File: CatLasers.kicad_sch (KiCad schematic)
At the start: 3 parts, among them J2 Conn_01x04, J3 Conn_01x04, U2 ATTINY402-SSN

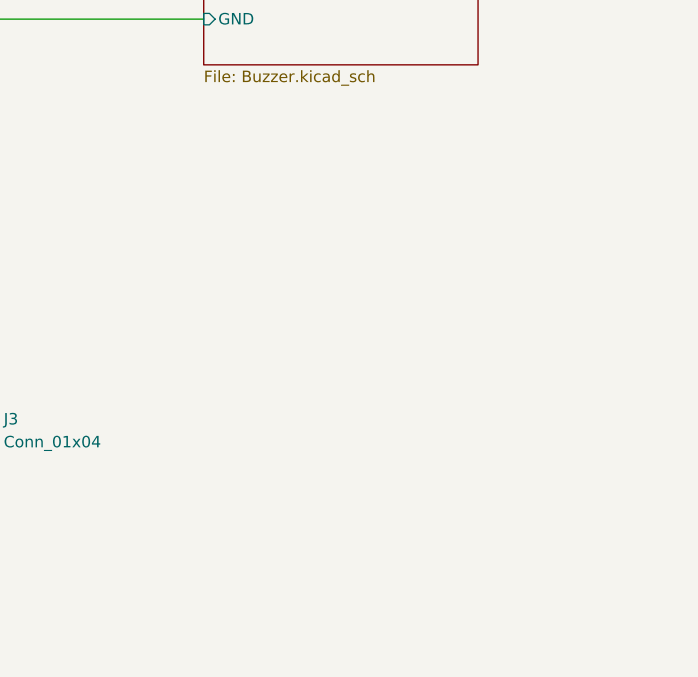
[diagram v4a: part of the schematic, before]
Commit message: IR Emitter circuit
Circuit added and all footprints assigned
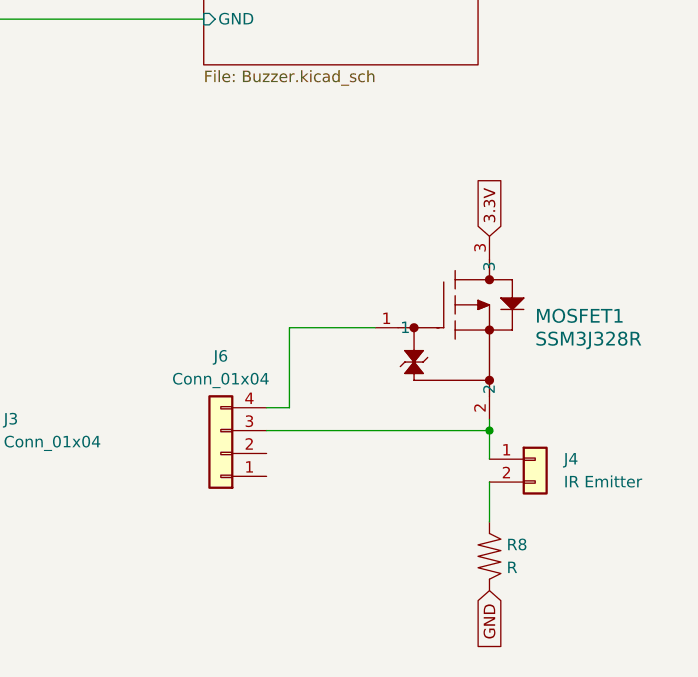
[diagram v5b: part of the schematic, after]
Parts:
- added J4: IR Emitter, Connector_PinHeader_2.54mm:PinHeader_1x02_P2.54mm_Vertical, symbol Connector_Generic:Conn_01x02
- added J6: Conn_01x04, Connector_PinHeader_2.54mm:PinHeader_1x04_P2.54mm_Vertical, symbol Connector_Generic:Conn_01x04
- added MOSFET1: SSM3J328R, SOT-23F_TOS, symbol ProjPMOS_LV:SSM3J328R
- added R8: R, Resistor_SMD:R_0805_2012Metric, symbol Hestres_Standard_Lib:R
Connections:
- net 3.3V: now also MOSFET1.3
- net GND: now also R8.2
- new net: J4.2 (Pin_2), R8.1
- new net: J6.4 (Pin_4), MOSFET1.1
- new net: J4.1 (Pin_1), J6.3 (Pin_3), MOSFET1.2
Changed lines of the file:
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@@
   (junction (at 80.645 42.545) (diameter 0) (color 0 0 0 0)
   )
+  (junction (at 179.705 101.6) (diameter 0) (color 0 0 0 0)
+  )
   (junction (at 114.935 55.88) (diameter 0) (color 0 0 0 0)
   )
@@
     (stroke (width 0) (type default))
   )
+  (wire (pts (xy 179.705 100.33) (xy 179.705 101.6))
+    (stroke (width 0) (type default))
+  )
+  (wire (pts (xy 154.94 99.06) (xy 157.48 99.06))
+    (stroke (width 0) (type default))
+  )
+  (wire (pts (xy 179.705 101.6) (xy 179.705 104.775))
+    (stroke (width 0) (type default))
+  )
+  (wire (pts (xy 154.94 101.6) (xy 179.705 101.6))
+    (stroke (width 0) (type default))
+  )
   (wire (pts (xy 72.39 49.53) (xy 76.835 49.53))
     (stroke (width 0) (type default))
@@
   )
   (wire (pts (xy 72.39 55.88) (xy 114.935 55.88))
+    (stroke (width 0) (type default))
+  )
+  (wire (pts (xy 157.48 99.06) (xy 157.48 90.17))
+    (stroke (width 0) (type default))
+  )
+  (wire (pts (xy 157.48 90.17) (xy 167.005 90.17))
+    (stroke (width 0) (type default))
+  )
+  (wire (pts (xy 179.705 107.315) (xy 179.705 111.76))
     (stroke (width 0) (type default))
   )
@@
     )
   )
+  (global_label "3.3V" (shape input) (at 179.705 80.01 90) (fields_autoplaced)
+    (effects (font (size 1.27 1.27)) (justify left))
+    (property "Intersheetrefs" "${INTERSHEET_REFS}" (at 179.705 72.9124 90)
+      (effects (font (size 1.27 1.27)) (justify left) hide)
+    )
+  )
+  (global_label "GND" (shape input) (at 179.705 119.38 270) (fields_autoplaced)
+    (effects (font (size 1.27 1.27)) (justify right))
+    (property "Intersheetrefs" "${INTERSHEET_REFS}" (at 179.705 126.2357 90)
+      (effects (font (size 1.27 1.27)) (justify right) hide)
+    )
+  )
   (global_label "3.3V" (shape input) (at 76.835 49.53 0) (fields_autoplaced)
     (effects (font (size 1.27 1.27)) (justify left))
     (property "Intersheetrefs" "${INTERSHEET_REFS}" (at 83.9326 49.53 0)
       (effects (font (size 1.27 1.27)) (justify left) hide)
+    )
+  )
+  (symbol (lib_id "Hestres_Standard_Lib:R") (at 179.705 115.57 0) (unit 1)
+    (in_bom yes) (on_board yes) (dnp no) (fields_autoplaced)
+    (property "Reference" "R8" (at 181.61 114.3 0)
+      (effects (font (size 1.27 1.27)) (justify left))
+    )
+    (property "Value" "R" (at 181.61 116.84 0)
+      (effects (font (size 1.27 1.27)) (justify left))
+    )
+    (property "Footprint" "Resistor_SMD:R_0805_2012Metric" (at 177.927 115.57 90)
+      (effects (font (size 1.27 1.27)) hide)
+    )
+    (property "Datasheet" "~" (at 179.705 115.57 0)
+      (effects (font (size 1.27 1.27)) hide)
+    )
+    (pin "1")
+    (pin "2")
+    (instances
+      (project "CatLasers"
+        (path "/b94f5b10-ee0c-4425-b025-e3a8bb3cc7b0"
+          (reference "R8") (unit 1)
+        )
+      )
     )
   )
@@
         )
       )
+    )
+  )
+  (symbol (lib_id "ProjPMOS_LV:SSM3J328R") (at 169.545 82.55 0) (unit 1)
+    (in_bom yes) (on_board yes) (dnp no) (fields_autoplaced)
+    (property "Reference" "MOSFET1" (at 184.785 88.9 0)
+      (effects (font (size 1.524 1.524)) (justify left))
+    )
+    (property "Value" "SSM3J328R" (at 184.785 91.44 0)
+      (effects (font (size 1.524 1.524)) (justify left))
+    )
+    (property "Footprint" "SOT-23F_TOS" (at 169.545 82.55 0)
+      (effects (font (size 1.27 1.27) italic) hide)
+    )
+    (property "Datasheet" "SSM3J328R" (at 169.545 82.55 0)
+      (effects (font (size 1.27 1.27) italic) hide)
+    )
+    (pin "1")
+    (pin "2")
+    (pin "3")
+    (instances
+      (project "CatLasers"
+        (path "/b94f5b10-ee0c-4425-b025-e3a8bb3cc7b0"
+          (reference "MOSFET1") (unit 1)
+        )
+      )
+    )
+  )
+  (symbol (lib_id "Connector_Generic:Conn_01x04") (at 149.86 104.14 180) (unit 1)
+    (in_bom yes) (on_board yes) (dnp no) (fields_autoplaced)
+    (property "Reference" "J6" (at 149.86 93.345 0)
+      (effects (font (size 1.27 1.27)))
+    )
+    (property "Value" "Conn_01x04" (at 149.86 95.885 0)
+      (effects (font (size 1.27 1.27)))
+    )
+    (property "Footprint" "Connector_PinHeader_2.54mm:PinHeader_1x04_P2.54mm_Vertical" (at 149.86 104.14 0)
+      (effects (font (size 1.27 1.27)) hide)
+    )
+    (property "Datasheet" "~" (at 149.86 104.14 0)
+      (effects (font (size 1.27 1.27)) hide)
+    )
+    (pin "1")
+    (pin "2")
+    (pin "3")
+    (pin "4")
+    (instances
+      (project "CatLasers"
+        (path "/b94f5b10-ee0c-4425-b025-e3a8bb3cc7b0"
+          (reference "J6") (unit 1)
+        )
+      )
+    )
+  )
+  (symbol (lib_id "Connector_Generic:Conn_01x02") (at 184.785 104.775 0) (unit 1)
+    (in_bom yes) (on_board yes) (dnp no) (fields_autoplaced)
+    (property "Reference" "J4" (at 187.96 104.775 0)
+      (effects (font (size 1.27 1.27)) (justify left))
+    )
+    (property "Value" "IR Emitter" (at 187.96 107.315 0)
+      (effects (font (size 1.27 1.27)) (justify left))
+    )
+    (property "Footprint" "Connector_PinHeader_2.54mm:PinHeader_1x02_P2.54mm_Vertical" (at 184.785 104.775 0)
+      (effects (font (size 1.27 1.27)) hide)
+    )
+    (property "Datasheet" "~" (at 184.785 104.775 0)
+      (effects (font (size 1.27 1.27)) hide)
+    )
+    (pin "1")
+    (pin "2")
+    (instances
+      (project "CatLasers"
+        (path "/b94f5b10-ee0c-4425-b025-e3a8bb3cc7b0"
+          (reference "J4") (unit 1)
+        )
+      )

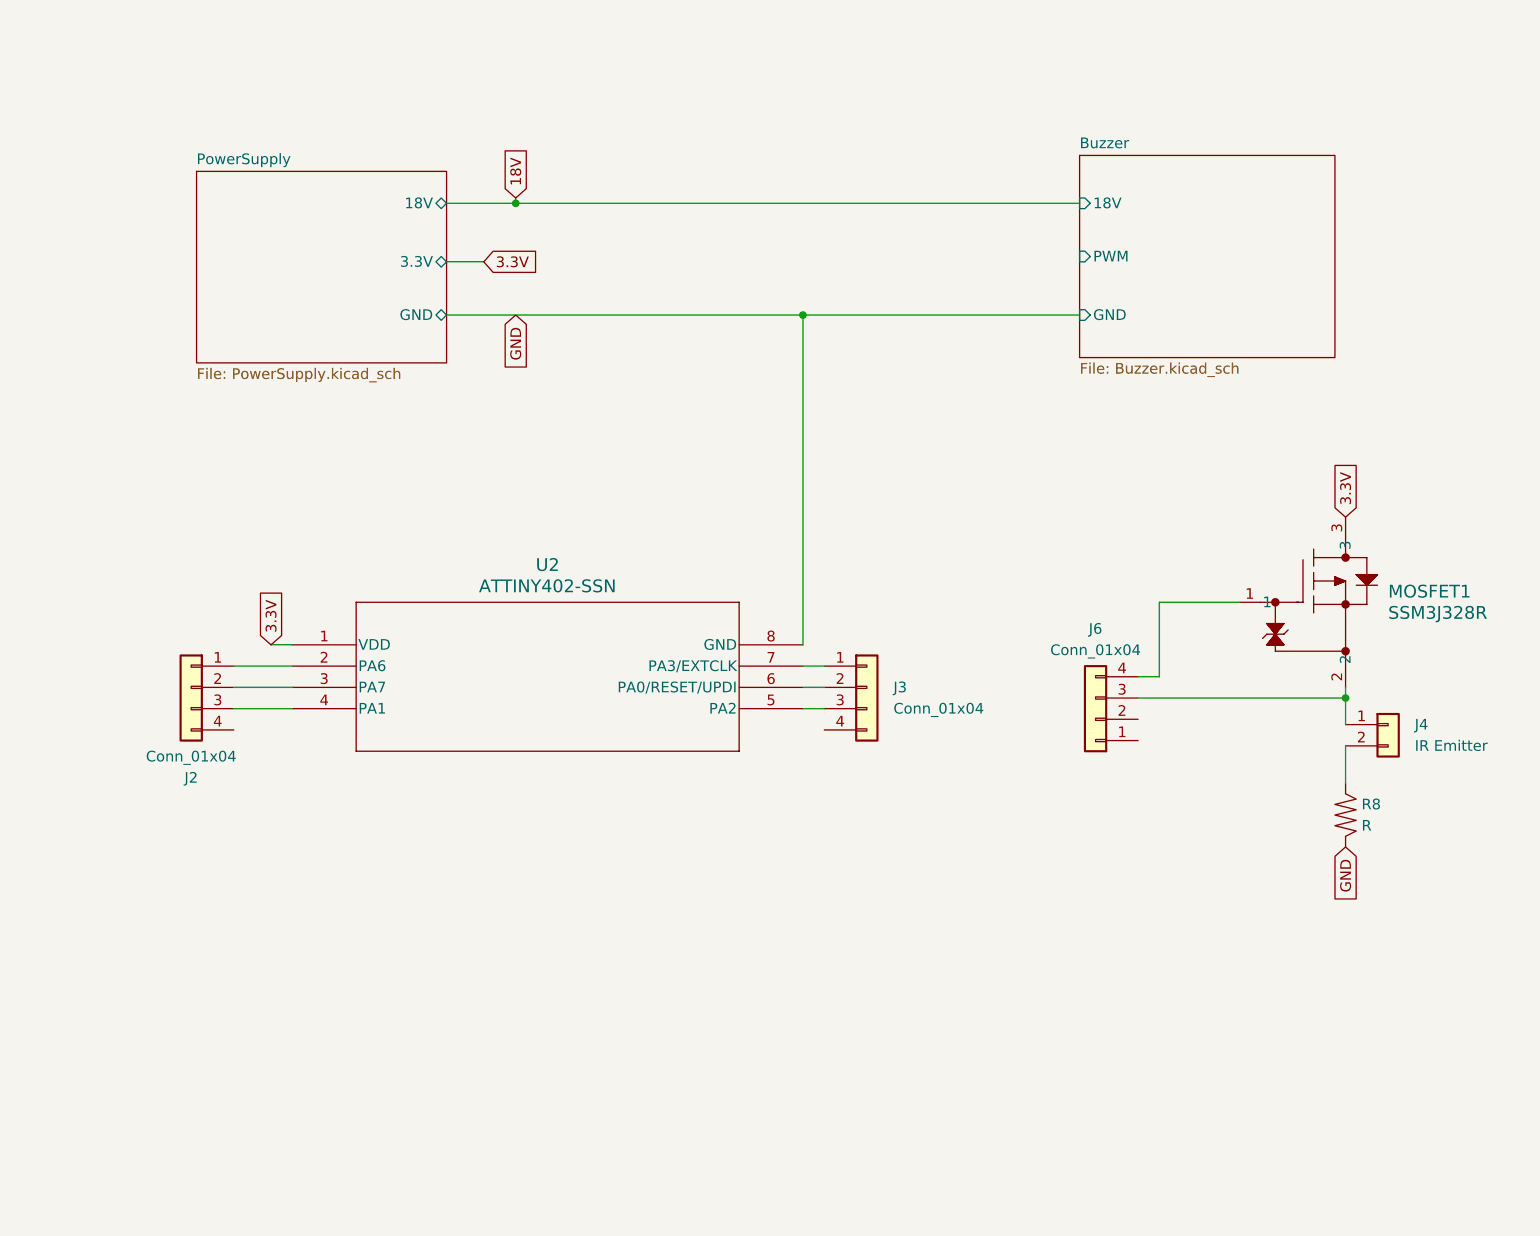
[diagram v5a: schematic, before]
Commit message: MCU switched to ESP32-WROOM
First pass at programmer pin connections
Footprints assigned
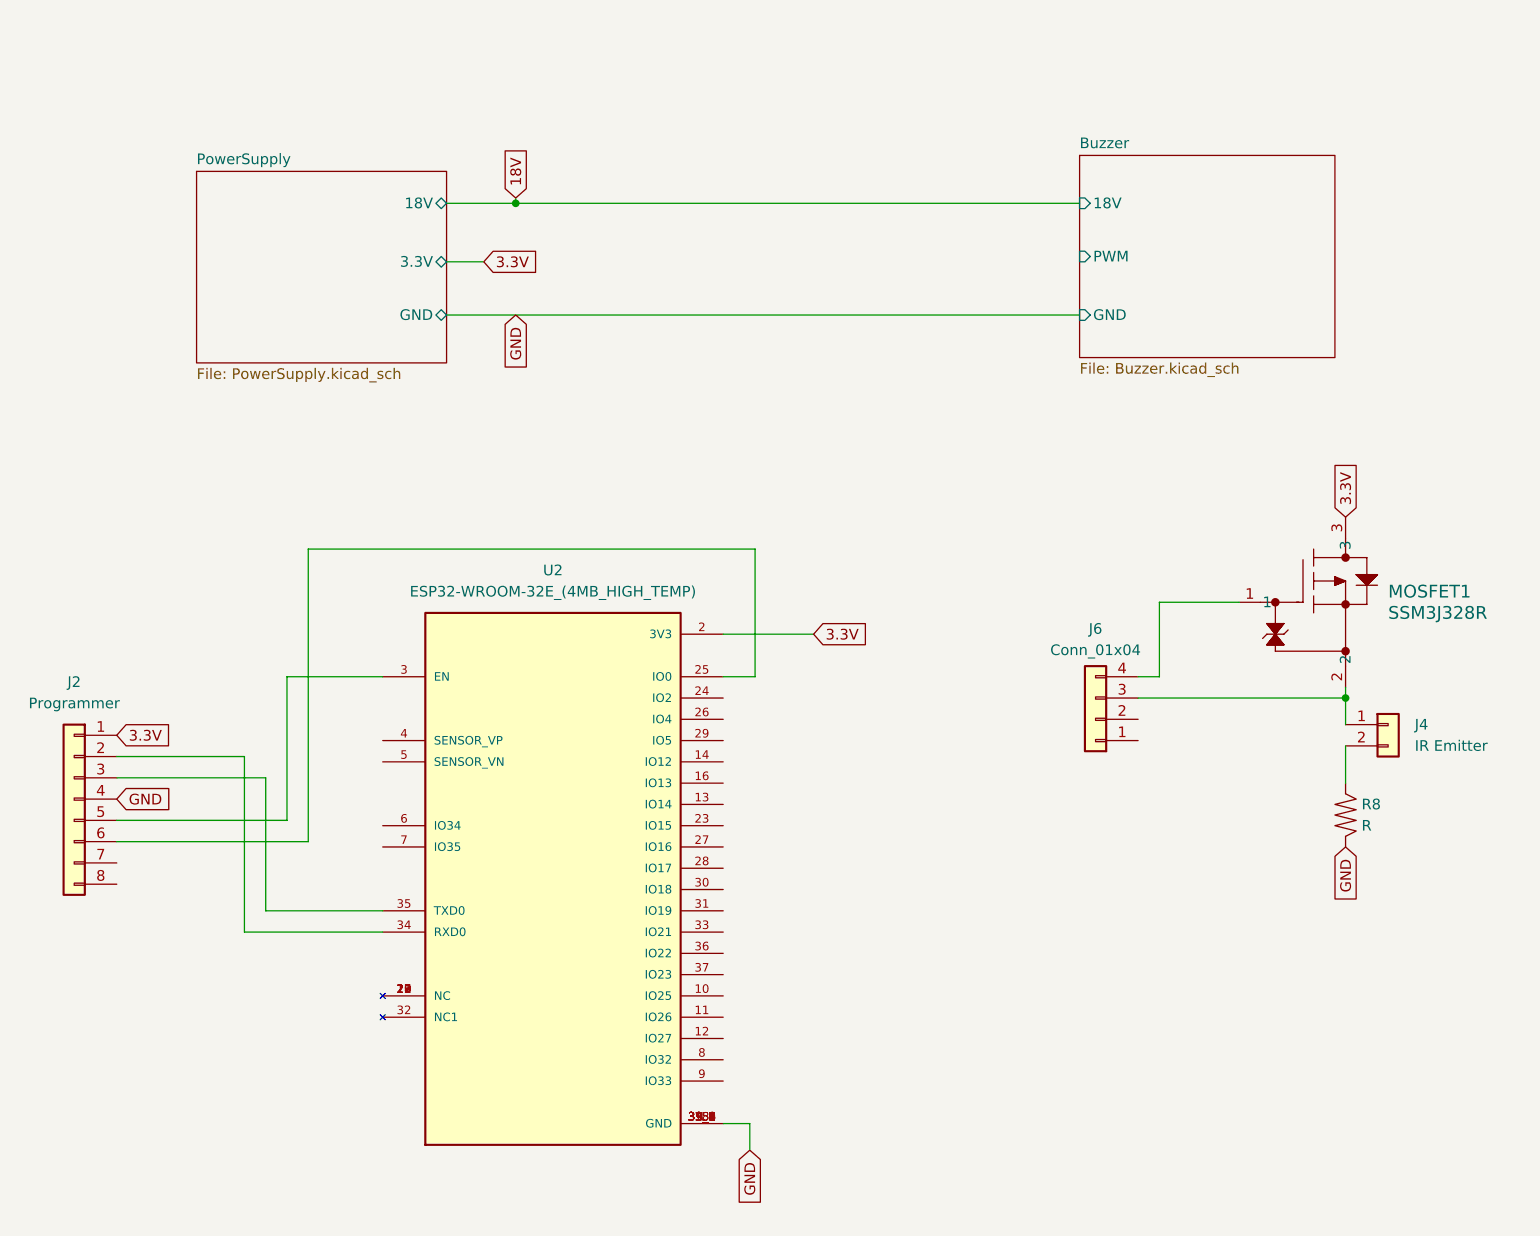
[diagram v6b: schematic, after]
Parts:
- removed J2, J3: Conn_01x04, Connector_PinHeader_2.54mm:PinHeader_1x04_P2.54mm_Vertical, symbol Connector_Generic:Conn_01x04
- removed U2: ATTINY402-SSN, symbol ProjMCU:ATTINY402-SSN
- added J2: Programmer, Connector_PinHeader_2.54mm:PinHeader_1x08_P2.54mm_Vertical, symbol Connector_Generic:Conn_01x08
- added U2: ESP32-WROOM-32E_(4MB_HIGH_TEMP), ESP32-WROOM-32E_(4MB_HIGH_TEMP):XCVR_ESP32-WROOM-32E_(4MB_HIGH_TEMP), symbol ProjMCU:ESP32-WROOM-32E_(4MB_HIGH_TEMP)
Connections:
- net 3.3V: now also J2.1 (Pin_1), U2.2 (3V3)
- net GND: now also J2.4 (Pin_4), U2.1 (GND), U2.15 (GND), U2.38 (GND), U2.39_1 (GND), U2.39_2 (GND), U2.39_3 (GND), U2.39_4 (GND), U2.39_5 (GND), U2.39_6 (GND), U2.39_7 (GND), U2.39_8 (GND), U2.39_9 (GND)
- new net: U2.17 (NC), U2.18 (NC), U2.19 (NC), U2.20 (NC), U2.21 (NC), U2.22 (NC)
- new net: J2.6 (Pin_6), U2.25 (IO0)
- new net: J2.5 (Pin_5), U2.3 (EN)
- new net: J2.2 (Pin_2), U2.34 (RXD0)
- new net: J2.3 (Pin_3), U2.35 (TXD0)
